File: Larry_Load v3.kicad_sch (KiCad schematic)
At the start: 72 parts, among them Q1 Q_NMOS_GDS, Q2 Q_NMOS_GDS, U1 TKISL21080DIH312Z-TK, U2 Opamp_Dual, U3 TPL5110, U4 TPS61222DCK

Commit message: Add files via upload
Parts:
- added RV1: 10 Turn Potentiometer, symbol Device:R_Potentiometer_US
- U1: value TKISL21080DIH312Z-TK -> REF3312AIDBZR
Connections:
- net CW: now also RV1.1
- net GND: now also RV1.3
- net WP: now also RV1.2
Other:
- note added: "Set for 1.000V at POT_CW Resistor array for series/parallel combo to trim value wihtout a trim pot"
- note removed: "Set for 1.000V at CW"
- note removed: "To 10-Turn Pot"
- moved on the sheet: C10, C3, R1, R2, TP1, TP10, TP2, TP20, TP3, TP5, TP6, TP7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

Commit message: Add files via upload
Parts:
- C5: value 100uF -> 47uF
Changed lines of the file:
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@@
 			)
 		)
-		(property "Value" "100uF"
+		(property "Value" "47uF"
 			(at 208.534 68.58 0)
 			(effects

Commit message: Add files via upload
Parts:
- RV1: value 10 Turn Potentiometer -> 30kΩ 10-Turn Potentiometer
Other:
- note added: "Battery traces on back panel"
- moved on the sheet: TP1, TP10, TP2, TP9
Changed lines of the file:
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@@
 	(wire
 		(pts
-			(xy 58.42 142.24) (xy 83.82 142.24)
+			(xy 58.42 151.13) (xy 83.82 151.13)
 		)
 		(stroke
@@
 	(wire
 		(pts
-			(xy 58.42 148.59) (xy 83.82 148.59)
+			(xy 58.42 157.48) (xy 83.82 157.48)
 		)
 		(stroke
@@
 	)
 	(rectangle
-		(start 33.655 73.66)
+		(start 25.4 73.66)
 		(end 66.675 88.265)
 		(stroke
@@
 		)
 	)
+	(rectangle
+		(start 51.435 134.62)
+		(end 98.425 160.655)
+		(stroke
+			(width 0)
+			(type default)
+		)
+		(fill
+			(type none)
+		)
+	)
 	(text "Off Board"
 		(exclude_from_sim no)
@@
 		)
 	)
+	(text "Battery traces on back panel"
+		(exclude_from_sim no)
+		(at 73.406 138.43 0)
+		(effects
+			(font
+				(size 1.27 1.27)
+			)
+		)
+	)
 	(text "Off Board"
 		(exclude_from_sim no)
@@
 	)
 	(label "B-"
-		(at 71.12 148.59 0)
+		(at 71.12 157.48 0)
 		(fields_autoplaced yes)
 		(effects
@@
 	)
 	(label "B+"
-		(at 69.85 142.24 0)
+		(at 69.85 151.13 0)
 		(fields_autoplaced yes)
 		(effects
@@
 	(symbol
 		(lib_id "Connector:TestPoint")
-		(at 83.82 148.59 0)
+		(at 83.82 157.48 0)
 		(unit 1)
 		(exclude_from_sim no)
@@
 		(fields_autoplaced yes)
 		(property "Reference" "TP10"
-			(at 86.36 144.0179 0)
+			(at 86.36 152.9079 0)
 			(effects
 				(font
@@
 		)
 		(property "Value" "TestPoint"
-			(at 86.36 146.5579 0)
+			(at 86.36 155.4479 0)
 			(effects
 				(font
@@
 		)
 		(property "Footprint" "0_Custom_Footprints:TestPoint_Pad_4.0x6.0mm"
-			(at 88.9 148.59 0)
+			(at 88.9 157.48 0)
 			(effects
 				(font
@@
 		)
 		(property "Datasheet" "~"
-			(at 88.9 148.59 0)
+			(at 88.9 157.48 0)
 			(effects
 				(font
@@
 		)
 		(property "Description" "test point"
-			(at 83.82 148.59 0)
+			(at 83.82 157.48 0)
 			(effects
 				(font
@@
 	(symbol
 		(lib_id "Connector:TestPoint")
-		(at 58.42 148.59 0)
+		(at 58.42 157.48 0)
 		(unit 1)
 		(exclude_from_sim no)
@@
 		(fields_autoplaced yes)
 		(property "Reference" "TP2"
-			(at 60.96 144.0179 0)
+			(at 60.96 152.9079 0)
 			(effects
 				(font
@@
 		)
 		(property "Value" "TestPoint"
-			(at 60.96 146.5579 0)
+			(at 60.96 155.4479 0)
 			(effects
 				(font
@@
 		)
 		(property "Footprint" "0_Custom_Footprints:TestPoint_Pad_4.0x6.0mm"
-			(at 63.5 148.59 0)
+			(at 63.5 157.48 0)
 			(effects
 				(font
@@
 		)
 		(property "Datasheet" "~"
-			(at 63.5 148.59 0)
+			(at 63.5 157.48 0)
 			(effects
 				(font
@@
 		)
 		(property "Description" "test point"
-			(at 58.42 148.59 0)
+			(at 58.42 157.48 0)
 			(effects
 				(font
@@
 			)
 		)
-		(property "Value" "10 Turn Potentiometer"
+		(property "Value" "30kΩ 10-Turn Potentiometer"
 			(at 59.182 81.534 0)
 			(effects
@@
 	(symbol
 		(lib_id "Connector:TestPoint")
-		(at 83.82 142.24 0)
+		(at 83.82 151.13 0)
 		(unit 1)
 		(exclude_from_sim no)
@@
 		(fields_autoplaced yes)
 		(property "Reference" "TP9"
-			(at 86.36 137.6679 0)
+			(at 86.36 146.5579 0)
 			(effects
 				(font
@@
 		)
 		(property "Value" "TestPoint"
-			(at 86.36 140.2079 0)
+			(at 86.36 149.0979 0)
 			(effects
 				(font
@@
 		)
 		(property "Footprint" "0_Custom_Footprints:TestPoint_Pad_4.0x6.0mm"
-			(at 88.9 142.24 0)
+			(at 88.9 151.13 0)
 			(effects
 				(font
@@
 		)
 		(property "Datasheet" "~"
-			(at 88.9 142.24 0)
+			(at 88.9 151.13 0)
 			(effects
 				(font
@@
 		)
 		(property "Description" "test point"
-			(at 83.82 142.24 0)
+			(at 83.82 151.13 0)
 			(effects
 				(font
@@
 	(symbol
 		(lib_id "Connector:TestPoint")
-		(at 58.42 142.24 0)
+		(at 58.42 151.13 0)
 		(unit 1)
 		(exclude_from_sim no)
@@
 		(fields_autoplaced yes)
 		(property "Reference" "TP1"
-			(at 60.96 137.6679 0)
+			(at 60.96 146.5579 0)
 			(effects
 				(font
@@
 		)
 		(property "Value" "TestPoint"
-			(at 60.96 140.2079 0)
+			(at 60.96 149.0979 0)
 			(effects
 				(font
@@
 		)
 		(property "Footprint" "0_Custom_Footprints:TestPoint_Pad_4.0x6.0mm"
-			(at 63.5 142.24 0)
+			(at 63.5 151.13 0)
 			(effects
 				(font
@@
 		)
 		(property "Datasheet" "~"
-			(at 63.5 142.24 0)
+			(at 63.5 151.13 0)
 			(effects
 				(font
@@
 		)
 		(property "Description" "test point"
-			(at 58.42 142.24 0)
+			(at 58.42 151.13 0)
 			(effects
 				(font

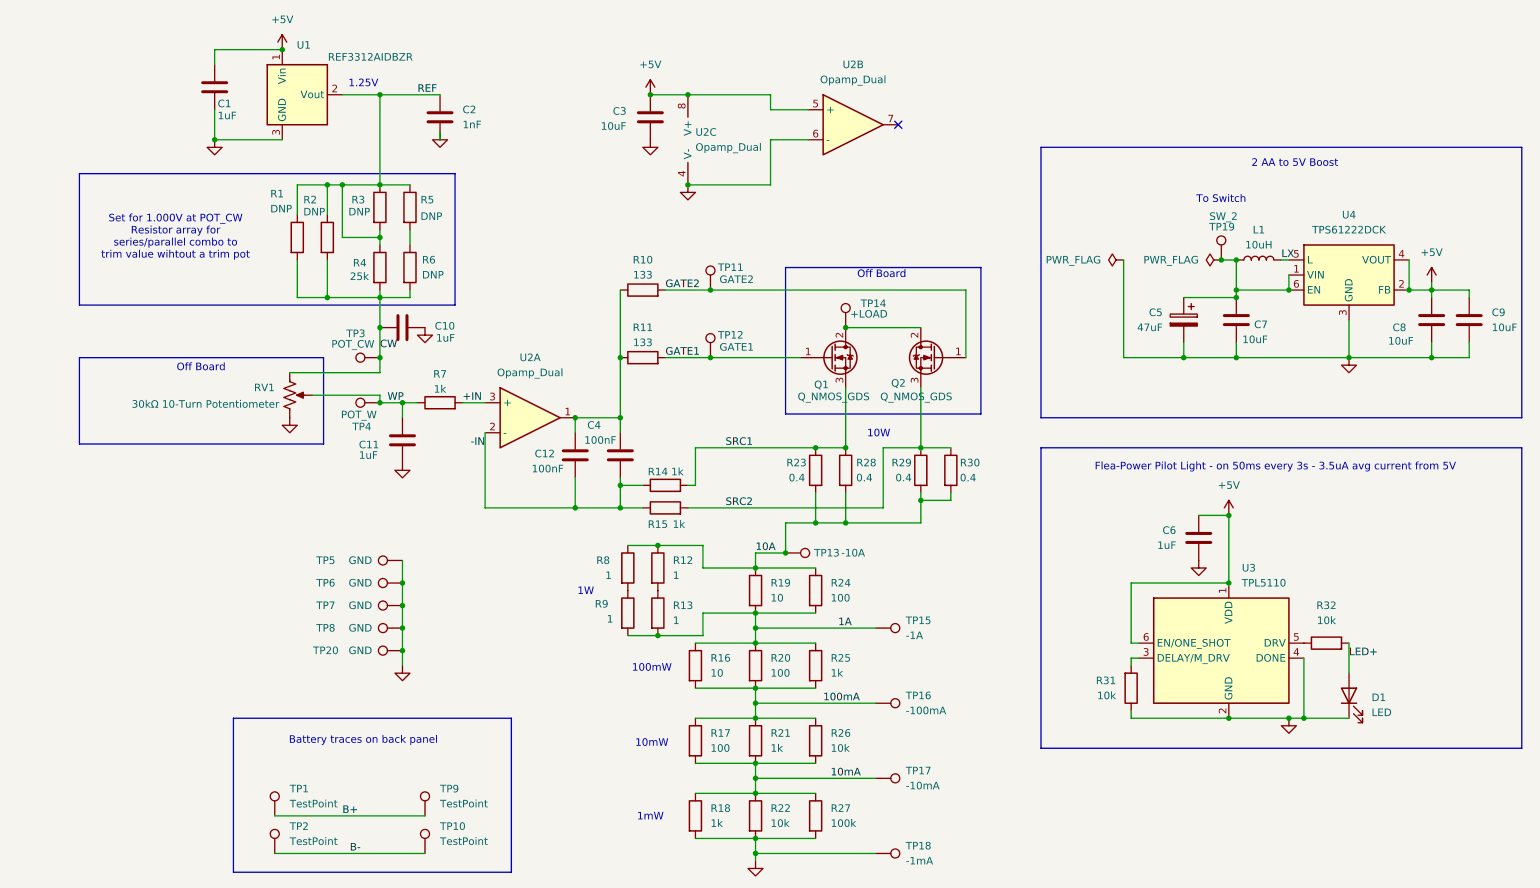
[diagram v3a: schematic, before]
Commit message: Add files via upload
Fixed incorrect values for LED blinker
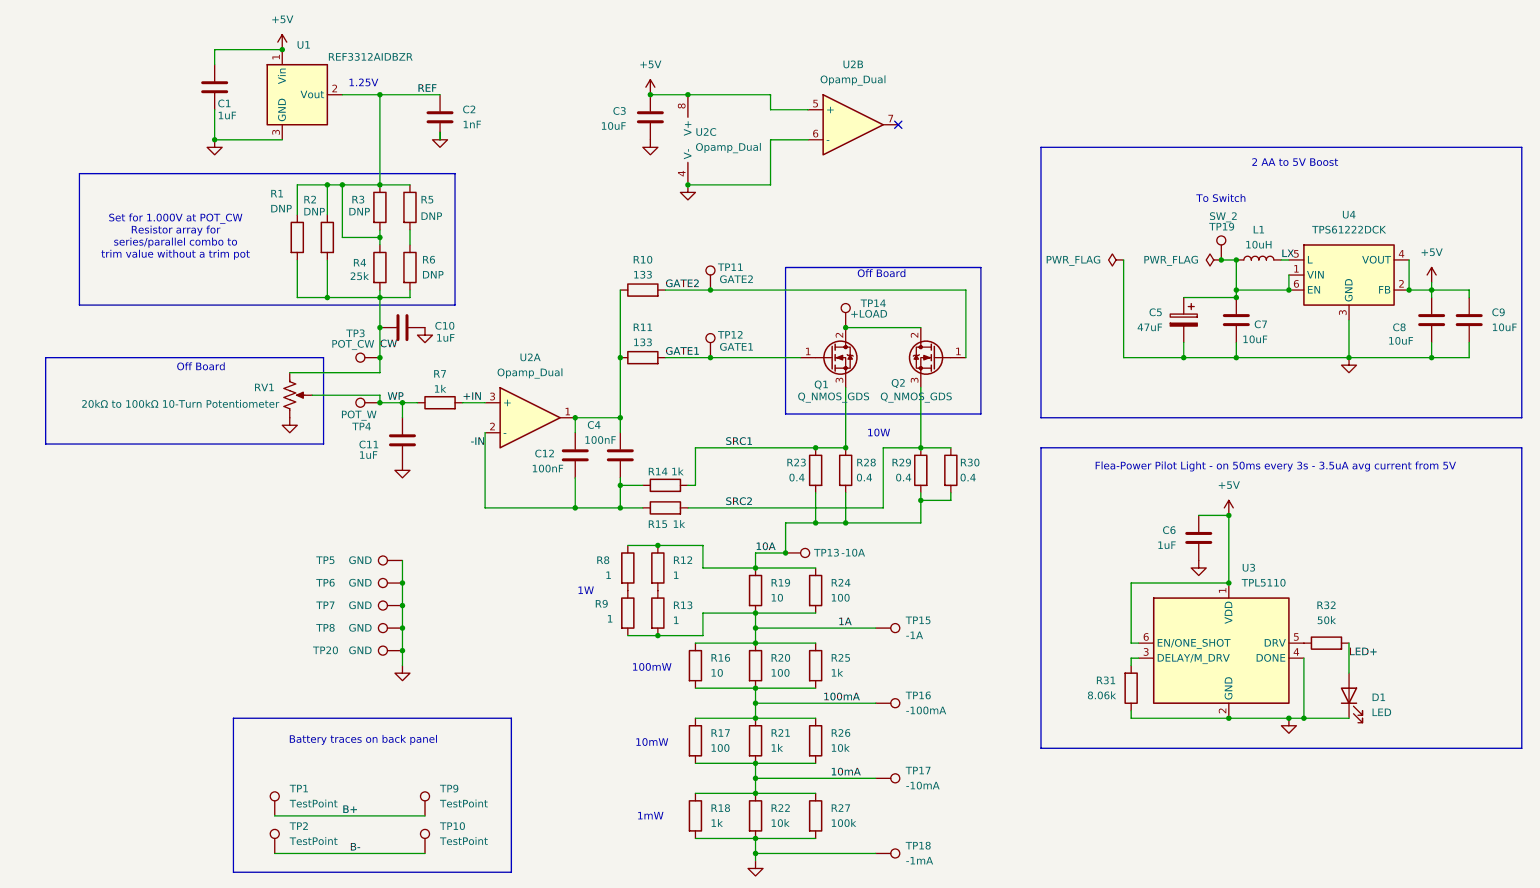
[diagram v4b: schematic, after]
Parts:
- R31: value 10k -> 8.06k
- R32: value 10k -> 50k
- RV1: value 30kΩ 10-Turn Potentiometer -> 20kΩ to 100kΩ 10-Turn Potentiometer
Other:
- note added: "Set for 1.000V at POT_CW Resistor array for series/parallel combo to trim value without a trim pot"
- note removed: "Set for 1.000V at POT_CW Resistor array for series/parallel combo to trim value wihtout a trim pot"
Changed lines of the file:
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@@
 	)
 	(rectangle
-		(start 25.4 73.66)
+		(start 19.685 73.66)
 		(end 66.675 88.265)
 		(stroke
@@
 		)
 	)
-	(text "Set for 1.000V at POT_CW\nResistor array for \nseries/parallel combo to \ntrim value wihtout a trim pot"
+	(text "Set for 1.000V at POT_CW\nResistor array for \nseries/parallel combo to \ntrim value without a trim pot"
 		(exclude_from_sim no)
 		(at 41.656 53.34 0)
@@
 			)
 		)
-		(property "Value" "30kΩ 10-Turn Potentiometer"
+		(property "Value" "20kΩ to 100kΩ 10-Turn Potentiometer"
 			(at 59.182 81.534 0)
 			(effects
@@
 			)
 		)
-		(property "Value" "10k"
+		(property "Value" "8.06k"
 			(at 200.66 130.8099 0)
 			(effects
@@
 			)
 		)
-		(property "Value" "10k"
+		(property "Value" "50k"
 			(at 236.22 118.11 90)
 			(effects
